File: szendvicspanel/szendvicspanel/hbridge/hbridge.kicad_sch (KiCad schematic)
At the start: 12 parts, among them J1 Conn_01x03_Pin, J2 Conn_01x02_Socket, Q1 BS170, Q2 BS170, Q3 BS170, Q4 BS170, Q5 BS250, Q6 BS250

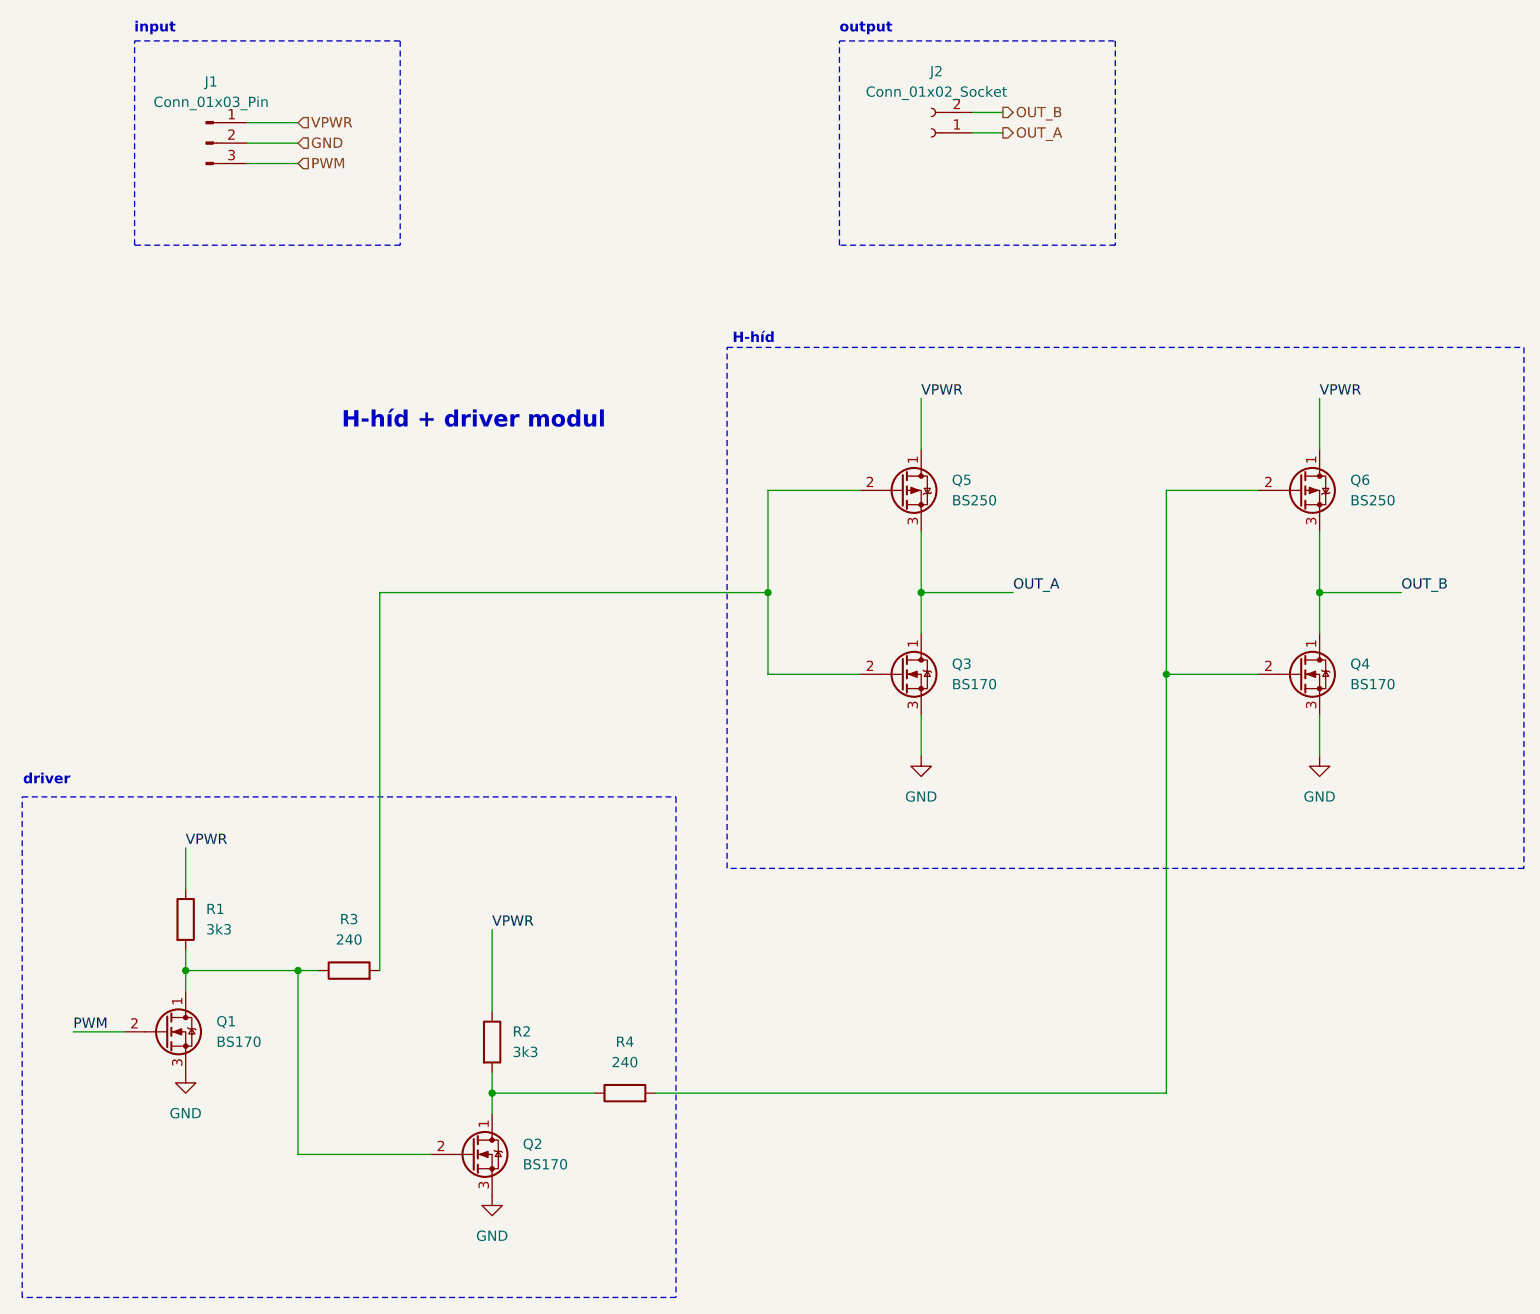
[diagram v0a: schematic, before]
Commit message: Átstrukturálás hierarchikus PCB-hez
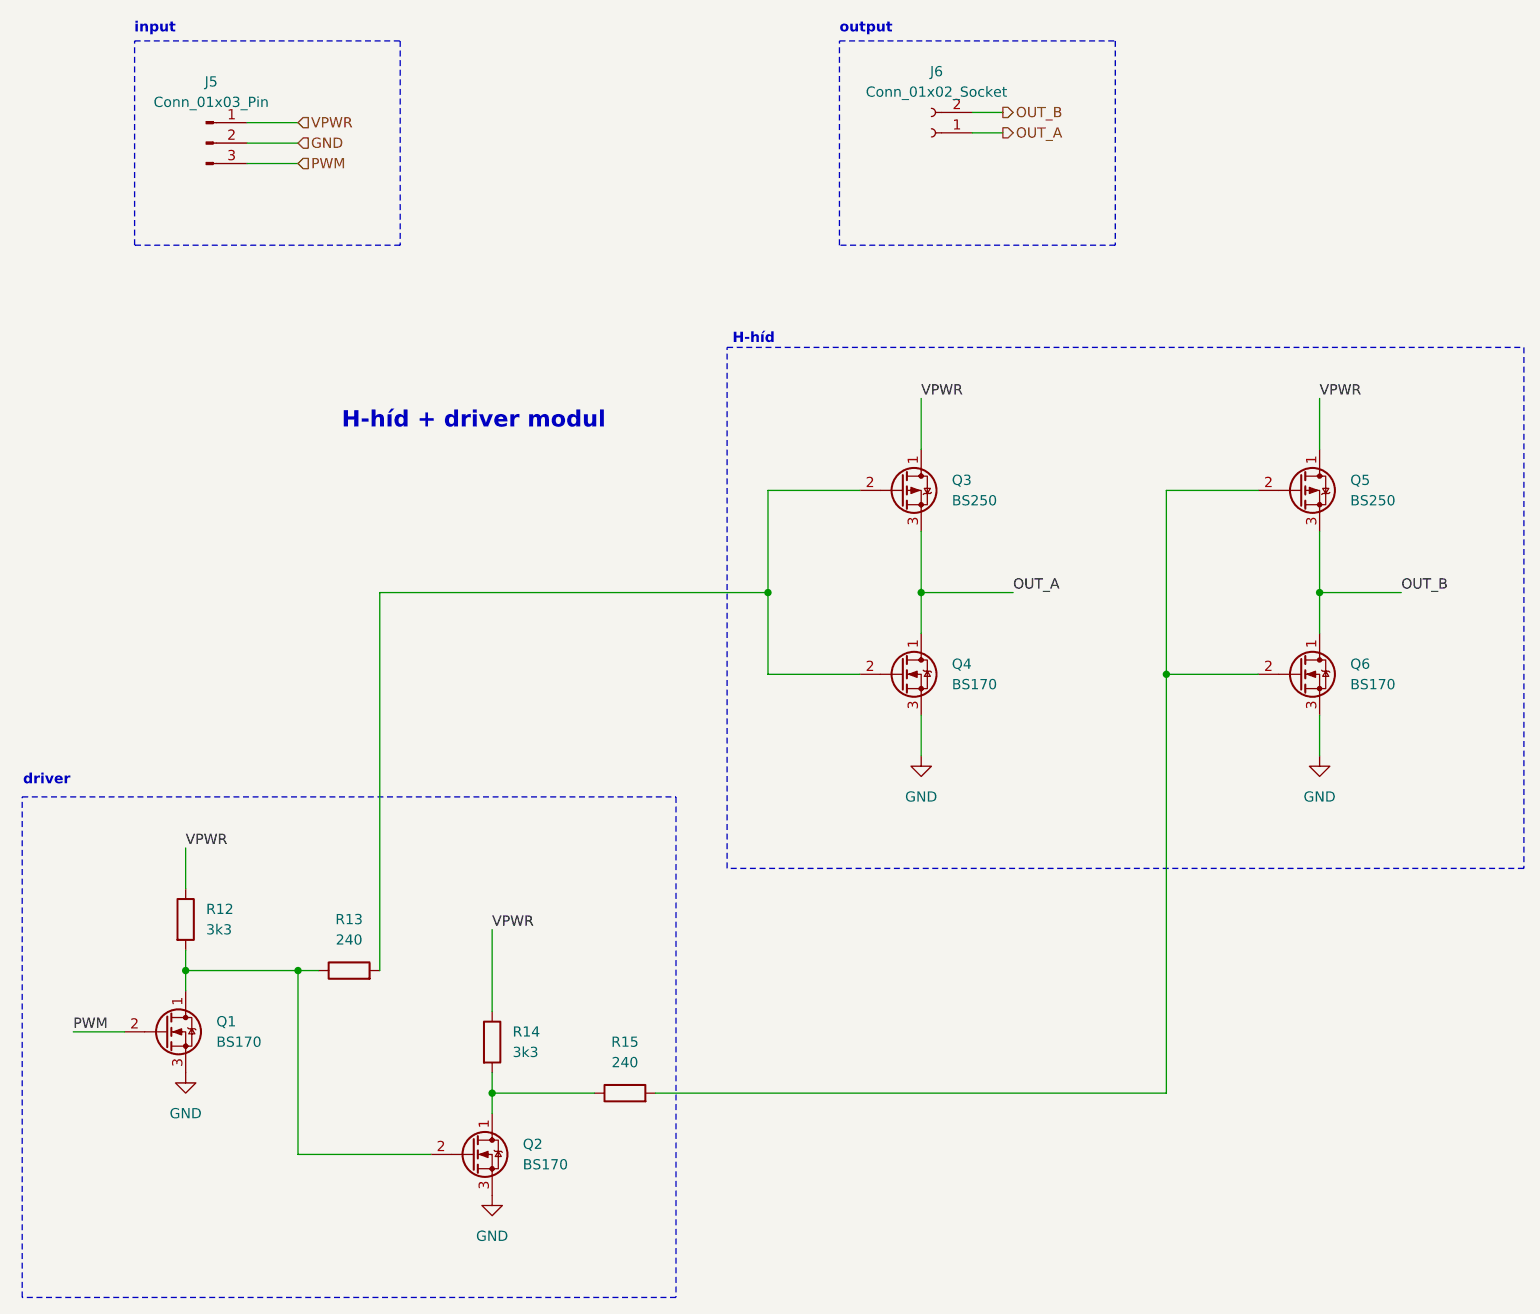
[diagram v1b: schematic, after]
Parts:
- renumbered J1 to J5, J2 to J6, Q5 to Q3, Q3 to Q4, Q6 to Q5, Q4 to Q6, R1 to R12, R3 to R13, R2 to R14, R4 to R15
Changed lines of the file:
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@@
 		(dnp no)
 		(fields_autoplaced yes)
-		(property "Reference" "#PWR04"
+		(property "Reference" "#PWR023"
 			(at 44.45 165.1 0)
 			(effects
@@
 			(project ""
 				(path "/2e536be4-7a69-4064-ab31-c73232c2dcfe/b7fbd7b6-659a-4f89-885b-600b77c2197e"
-					(reference "#PWR04")
+					(reference "#PWR023")
 					(unit 1)
 				)
@@
 		(dnp no)
 		(fields_autoplaced yes)
-		(property "Reference" "Q6"
+		(property "Reference" "Q5"
 			(at 189.23 85.0899 0)
 			(effects
@@
 			(project ""
 				(path "/2e536be4-7a69-4064-ab31-c73232c2dcfe/b7fbd7b6-659a-4f89-885b-600b77c2197e"
-					(reference "Q6")
+					(reference "Q5")
 					(unit 1)
 				)
@@
 		(dnp no)
 		(fields_autoplaced yes)
-		(property "Reference" "Q3"
+		(property "Reference" "Q4"
 			(at 139.7 107.9499 0)
 			(effects
@@
 			(project "szendvicspanel"
 				(path "/2e536be4-7a69-4064-ab31-c73232c2dcfe/b7fbd7b6-659a-4f89-885b-600b77c2197e"
-					(reference "Q3")
+					(reference "Q4")
 					(unit 1)
 				)
@@
 		(dnp no)
 		(fields_autoplaced yes)
-		(property "Reference" "#PWR05"
+		(property "Reference" "#PWR024"
 			(at 82.55 180.34 0)
 			(effects
@@
 			(project ""
 				(path "/2e536be4-7a69-4064-ab31-c73232c2dcfe/b7fbd7b6-659a-4f89-885b-600b77c2197e"
-					(reference "#PWR05")
+					(reference "#PWR024")
 					(unit 1)
 				)
@@
 		(dnp no)
 		(fields_autoplaced yes)
-		(property "Reference" "R2"
+		(property "Reference" "R14"
 			(at 85.09 153.6699 0)
 			(effects
@@
 			(project ""
 				(path "/2e536be4-7a69-4064-ab31-c73232c2dcfe/b7fbd7b6-659a-4f89-885b-600b77c2197e"
-					(reference "R2")
+					(reference "R14")
 					(unit 1)
 				)
@@
 		(dnp no)
 		(fields_autoplaced yes)
-		(property "Reference" "R4"
+		(property "Reference" "R15"
 			(at 99.06 154.94 90)
 			(effects
@@
 			(project "szendvicspanel"
 				(path "/2e536be4-7a69-4064-ab31-c73232c2dcfe/b7fbd7b6-659a-4f89-885b-600b77c2197e"
-					(reference "R4")
+					(reference "R15")
 					(unit 1)
 				)
@@
 		(dnp no)
 		(fields_autoplaced yes)
-		(property "Reference" "J1"
+		(property "Reference" "J5"
 			(at 47.625 35.56 0)
 			(effects
@@
 			(project ""
 				(path "/2e536be4-7a69-4064-ab31-c73232c2dcfe/b7fbd7b6-659a-4f89-885b-600b77c2197e"
-					(reference "J1")
+					(reference "J5")
 					(unit 1)
 				)
@@
 		(dnp no)
 		(fields_autoplaced yes)
-		(property "Reference" "#PWR07"
+		(property "Reference" "#PWR026"
 			(at 185.42 125.73 0)
 			(effects
@@
 			(project ""
 				(path "/2e536be4-7a69-4064-ab31-c73232c2dcfe/b7fbd7b6-659a-4f89-885b-600b77c2197e"
-					(reference "#PWR07")
+					(reference "#PWR026")
 					(unit 1)
 				)
@@
 		(dnp no)
 		(fields_autoplaced yes)
-		(property "Reference" "Q4"
+		(property "Reference" "Q6"
 			(at 189.23 107.9499 0)
 			(effects
@@
 			(project "szendvicspanel"
 				(path "/2e536be4-7a69-4064-ab31-c73232c2dcfe/b7fbd7b6-659a-4f89-885b-600b77c2197e"
-					(reference "Q4")
+					(reference "Q6")
 					(unit 1)
 				)
@@
 		(dnp no)
 		(fields_autoplaced yes)
-		(property "Reference" "R1"
+		(property "Reference" "R12"
 			(at 46.99 138.4299 0)
 			(effects
@@
 			(project ""
 				(path "/2e536be4-7a69-4064-ab31-c73232c2dcfe/b7fbd7b6-659a-4f89-885b-600b77c2197e"
-					(reference "R1")
+					(reference "R12")
 					(unit 1)
 				)
@@
 		(dnp no)
 		(fields_autoplaced yes)
-		(property "Reference" "#PWR06"
+		(property "Reference" "#PWR025"
 			(at 135.89 125.73 0)
 			(effects
@@
 			(project ""
 				(path "/2e536be4-7a69-4064-ab31-c73232c2dcfe/b7fbd7b6-659a-4f89-885b-600b77c2197e"
-					(reference "#PWR06")
+					(reference "#PWR025")
 					(unit 1)
 				)
@@
 		(dnp no)
 		(fields_autoplaced yes)
-		(property "Reference" "Q5"
+		(property "Reference" "Q3"
 			(at 139.7 85.0899 0)
 			(effects
@@
 			(project ""
 				(path "/2e536be4-7a69-4064-ab31-c73232c2dcfe/b7fbd7b6-659a-4f89-885b-600b77c2197e"
-					(reference "Q5")
+					(reference "Q3")
 					(unit 1)
 				)
@@
 		(dnp no)
 		(fields_autoplaced yes)
-		(property "Reference" "J2"
+		(property "Reference" "J6"
 			(at 137.795 34.29 0)
 			(effects
@@
 			(project ""
 				(path "/2e536be4-7a69-4064-ab31-c73232c2dcfe/b7fbd7b6-659a-4f89-885b-600b77c2197e"
-					(reference "J2")
+					(reference "J6")
 					(unit 1)
 				)
@@
 		(dnp no)
 		(fields_autoplaced yes)
-		(property "Reference" "R3"
+		(property "Reference" "R13"
 			(at 64.77 139.7 90)
 			(effects
@@
 			(project ""
 				(path "/2e536be4-7a69-4064-ab31-c73232c2dcfe/b7fbd7b6-659a-4f89-885b-600b77c2197e"
-					(reference "R3")
-					(unit 1)
-				)
+					(reference "R13")
+					(unit 1)
+				)
